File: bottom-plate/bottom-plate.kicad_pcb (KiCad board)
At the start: 2 copper layers, 309.8 x 119.3 mm, 1 part

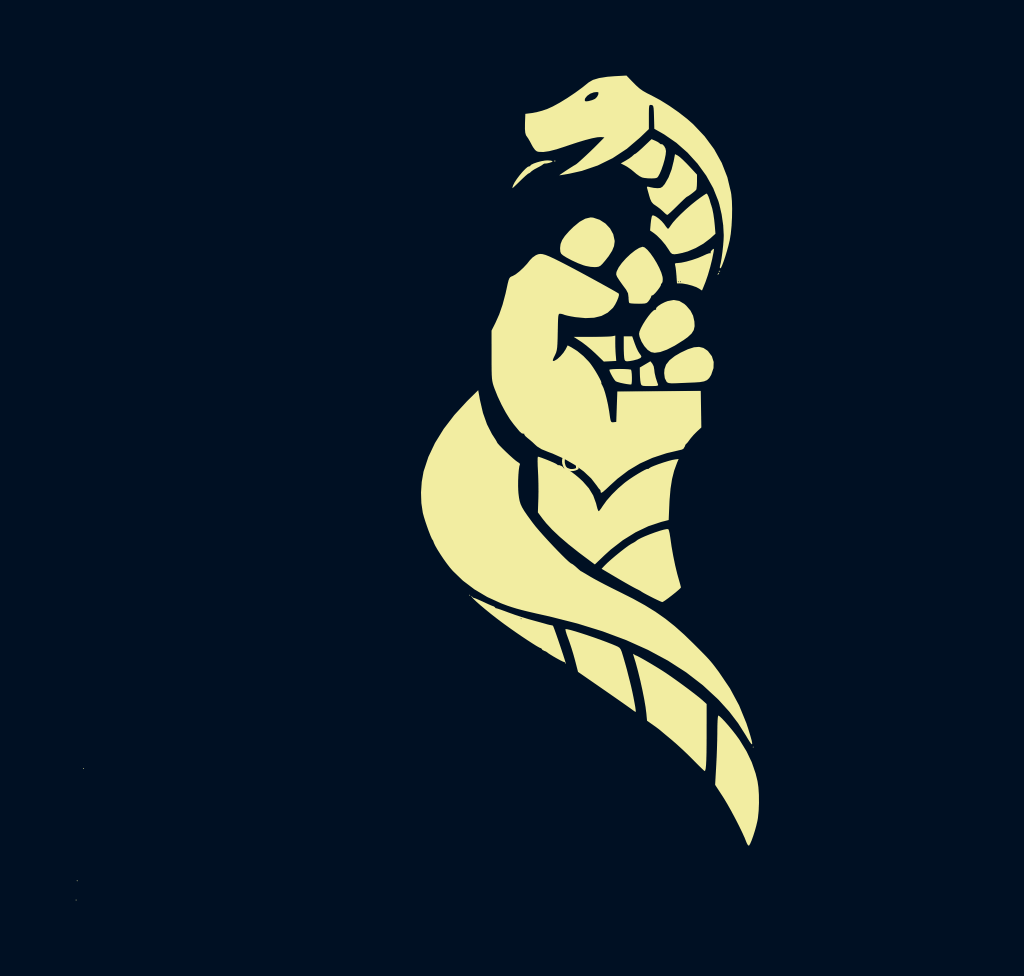
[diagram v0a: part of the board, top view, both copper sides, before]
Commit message: Drop references to the original design; dark grey modifier keycaps
- Main PCB project moves to pcb/polymetis.*; firmware crate, KLE layout,
  factory files, check reports and UF2 are named polymetis.
- Board text: the credit line is removed. Bottom plate: the old logo is
  replaced by Polymetis text on the outside face.
- Unused legacy files removed: KiCad 5 project, kbplacer log, FreeCAD
  frame, plate-generator outlines, the original handover brief. The
  frame script reads case/frame-source.stl.
- README, HANDOVER and CLAUDE.md no longer describe Polymetis as a fork.
  LICENSE is unchanged: the MIT terms require its copyright and
  permission notice to stay with the design.
- Keycaps: a sixth colour, dark grey (the body colour), for the 11
  modifiers; the layout page, concept model, layout image and renders
  are updated.

Co-Authored-By: Claude Opus 5.5 <noreply@anthropic.com>
Claude-Session: https://claude.ai/code/session_011sJxCFL16sEAYrBmNTBwJC
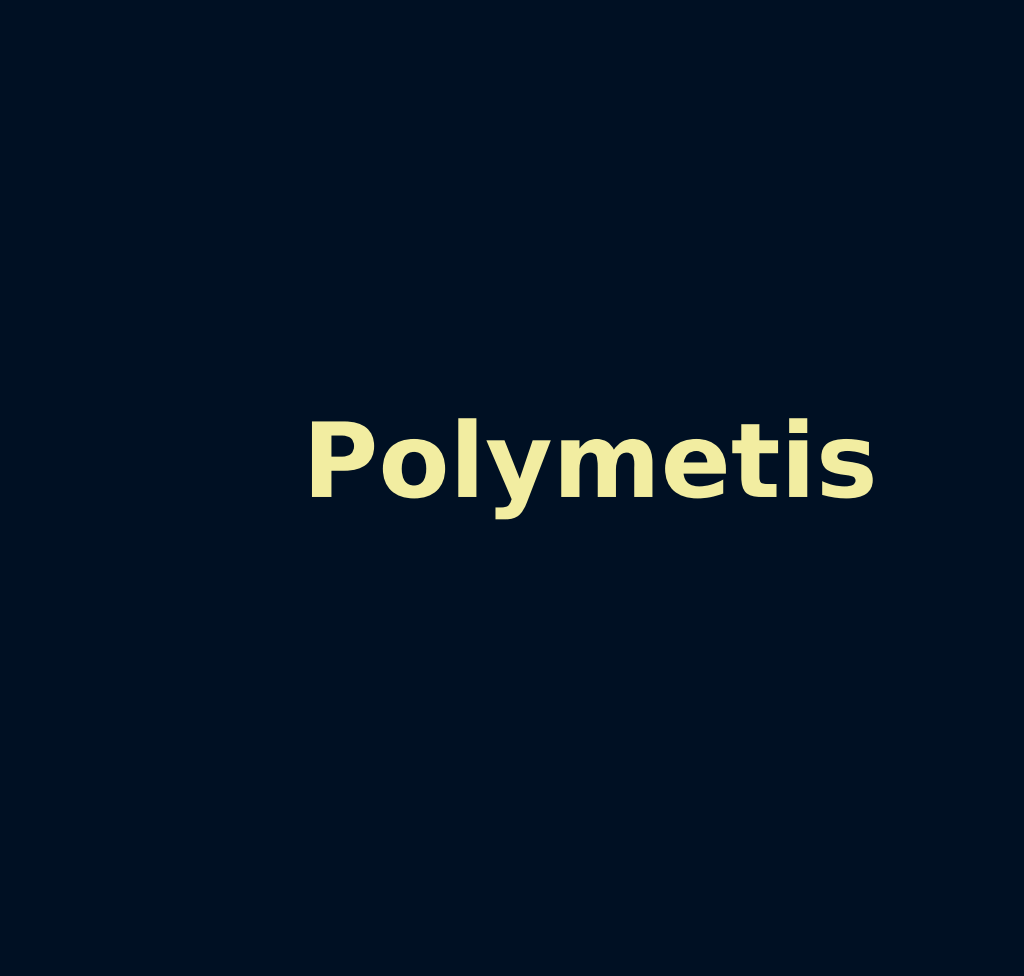
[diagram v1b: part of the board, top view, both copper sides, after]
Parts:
- removed G***: LOGO, local:boethia_logo
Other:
- board text added: "Polymetis"
